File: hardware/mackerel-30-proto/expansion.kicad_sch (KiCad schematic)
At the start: 4 parts, among them J14 DIN41612_03x32_ABC, U14 74HC245, U15 74HC245, U16 74HC245

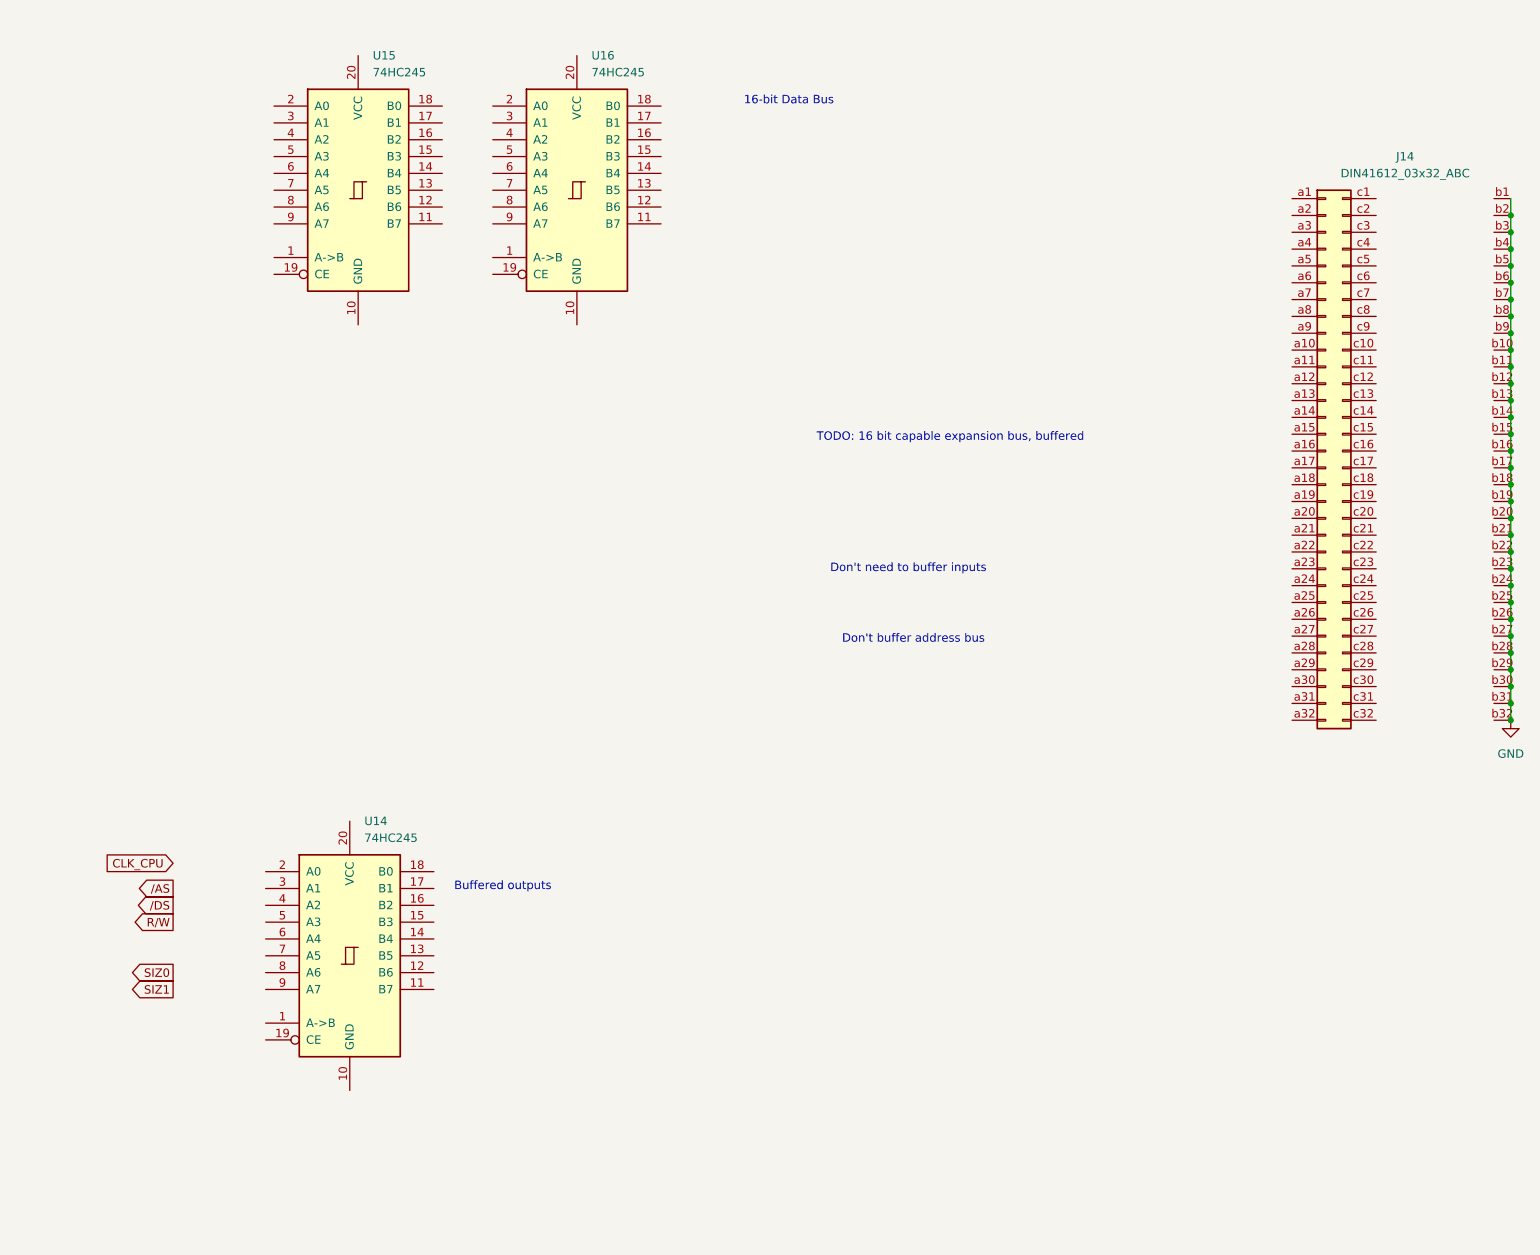
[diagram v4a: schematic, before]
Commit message: Mack-30 routed except for expansion header
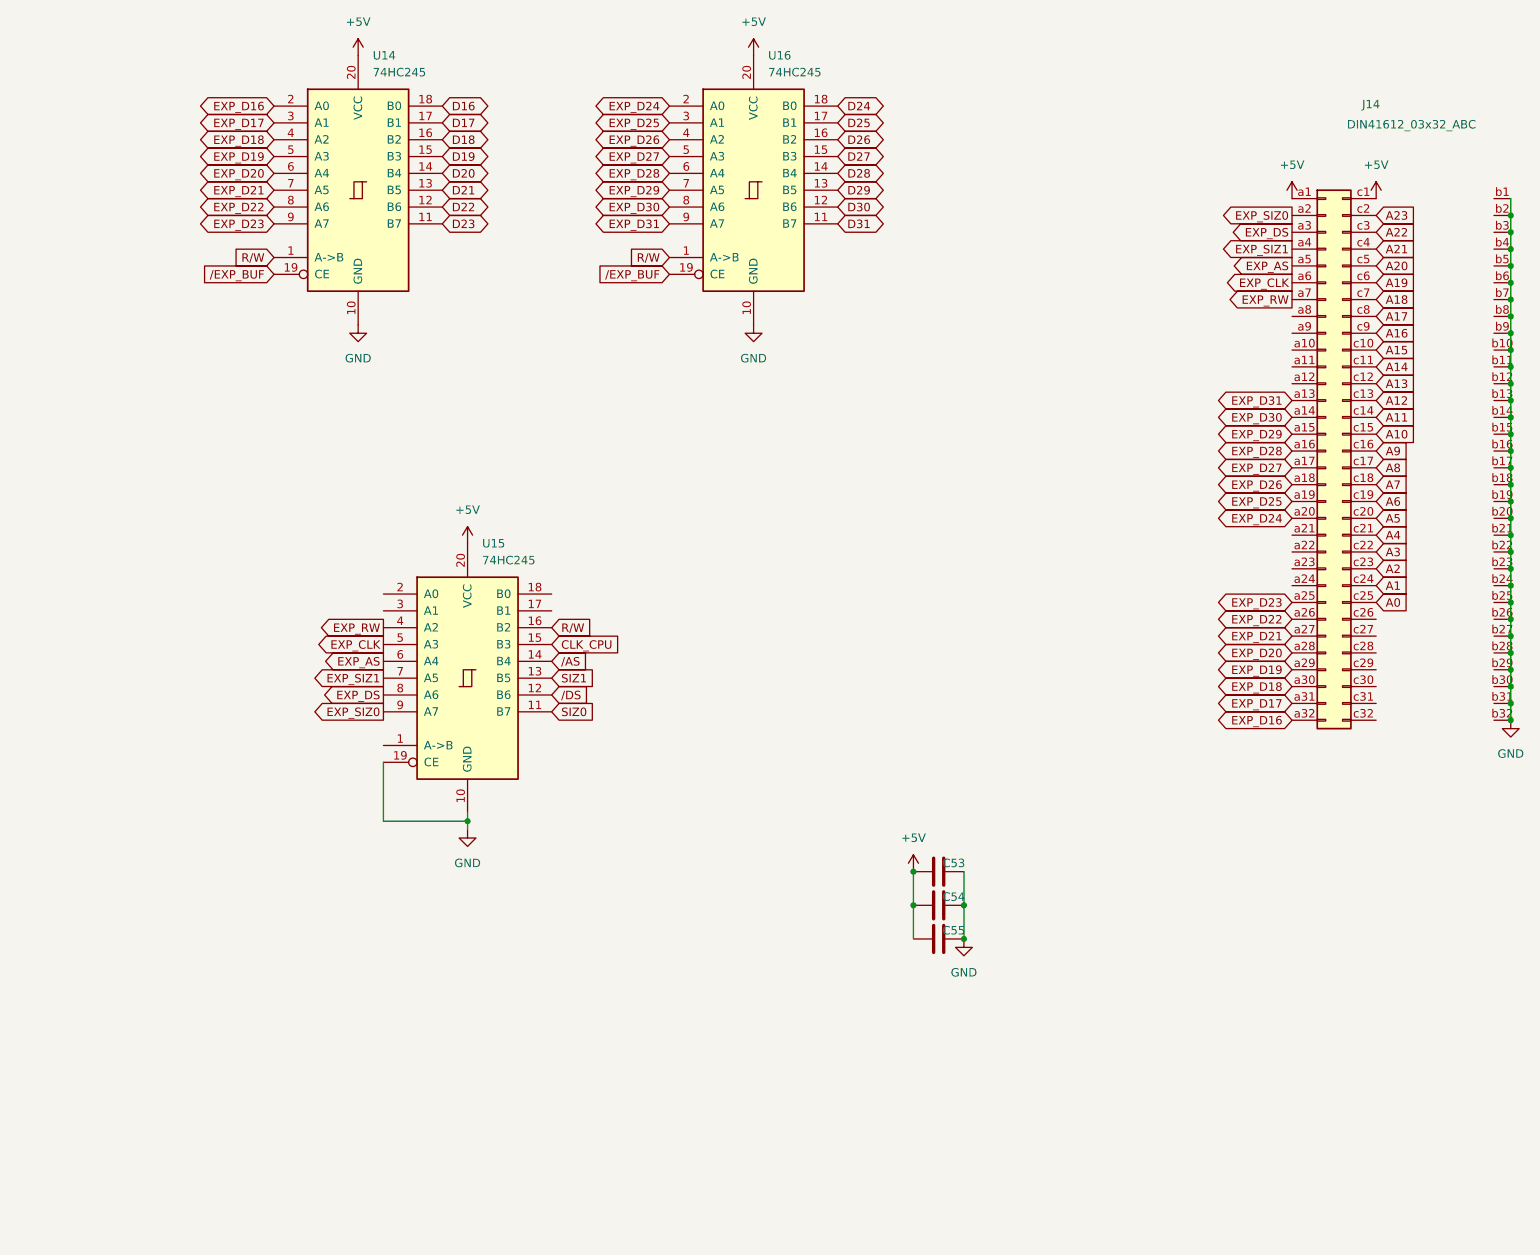
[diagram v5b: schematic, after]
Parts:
- added C53, C54, C55: 0.1uF, Capacitor_THT:C_Disc_D4.3mm_W1.9mm_P5.00mm, symbol Device:C
- renumbered U15 to U14, U14 to U15
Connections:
- net CLK_CPU: now also U15.15 (B3)
- net GND: now also U14.10 (GND), U15.10 (GND), U15.19 (CE), U16.10 (GND), C53.2, C54.2, C55.2
- net R/W: now also U14.1 (A->B), U15.16 (B2), U16.1 (A->B)
- net SIZ0: now also U15.11 (B7)
- net SIZ1: now also U15.13 (B5)
- net /AS: now also U15.14 (B4)
- net /DS: now also U15.12 (B6)
- net +5V: now reaches U15.20 (VCC)
- net +5V: now also J14.a1 (Pin_a1), J14.c1 (Pin_c1), U14.20 (VCC), U16.20 (VCC), C53.1, C54.1, C55.1
- net EXP_RW: now reaches U15.4 (A2)
- net EXP_RW: now also J14.a7 (Pin_a7)
- net EXP_CLK: now reaches U15.5 (A3)
- net EXP_CLK: now also J14.a6 (Pin_a6)
- net EXP_AS: now reaches U15.6 (A4)
- net EXP_AS: now also J14.a5 (Pin_a5)
- net EXP_SIZ1: now reaches U15.7 (A5)
- net EXP_SIZ1: now also J14.a4 (Pin_a4)
- net EXP_DS: now reaches U15.8 (A6)
- net EXP_DS: now also J14.a3 (Pin_a3)
- net EXP_SIZ0: now reaches U15.9 (A7)
- net EXP_SIZ0: now also J14.a2 (Pin_a2)
- net D23: now reaches U14.11 (B7)
- net D22: now reaches U14.12 (B6)
- net D21: now reaches U14.13 (B5)
- net D20: now reaches U14.14 (B4)
- net D19: now reaches U14.15 (B3)
- net D18: now reaches U14.16 (B2)
- net D17: now reaches U14.17 (B1)
- net D16: now reaches U14.18 (B0)
- net /EXP_BUF: now reaches U14.19 (CE)
- net /EXP_BUF: now also U16.19 (CE)
- net EXP_D16: now reaches U14.2 (A0)
- net EXP_D16: now also J14.a32 (Pin_a32)
- net EXP_D17: now reaches U14.3 (A1)
- net EXP_D17: now also J14.a31 (Pin_a31)
- net EXP_D18: now reaches U14.4 (A2)
- net EXP_D18: now also J14.a30 (Pin_a30)
- net EXP_D19: now reaches U14.5 (A3)
- net EXP_D19: now also J14.a29 (Pin_a29)
- net EXP_D20: now reaches U14.6 (A4)
- net EXP_D20: now also J14.a28 (Pin_a28)
- net EXP_D21: now reaches U14.7 (A5)
- net EXP_D21: now also J14.a27 (Pin_a27)
- net EXP_D22: now reaches U14.8 (A6)
- net EXP_D22: now also J14.a26 (Pin_a26)
- net EXP_D23: now reaches U14.9 (A7)
- net EXP_D23: now also J14.a25 (Pin_a25)
- net D31: now reaches U16.11 (B7)
- net D30: now reaches U16.12 (B6)
- net D29: now reaches U16.13 (B5)
- net D28: now reaches U16.14 (B4)
- net D27: now reaches U16.15 (B3)
- net D26: now reaches U16.16 (B2)
- net D25: now reaches U16.17 (B1)
- net D24: now reaches U16.18 (B0)
- net EXP_D24: now reaches U16.2 (A0)
- net EXP_D24: now also J14.a20 (Pin_a20)
- net EXP_D25: now reaches U16.3 (A1)
- net EXP_D25: now also J14.a19 (Pin_a19)
- net EXP_D26: now reaches U16.4 (A2)
- net EXP_D26: now also J14.a18 (Pin_a18)
- net EXP_D27: now reaches U16.5 (A3)
- net EXP_D27: now also J14.a17 (Pin_a17)
- net EXP_D28: now reaches U16.6 (A4)
- net EXP_D28: now also J14.a16 (Pin_a16)
- net EXP_D29: now reaches U16.7 (A5)
- net EXP_D29: now also J14.a15 (Pin_a15)
- net EXP_D30: now reaches U16.8 (A6)
- net EXP_D30: now also J14.a14 (Pin_a14)
- net EXP_D31: now reaches U16.9 (A7)
- net EXP_D31: now also J14.a13 (Pin_a13)
- net A15: now reaches J14.c10 (Pin_c10)
- net A14: now reaches J14.c11 (Pin_c11)
- net A13: now reaches J14.c12 (Pin_c12)
- net A12: now reaches J14.c13 (Pin_c13)
- net A11: now reaches J14.c14 (Pin_c14)
- net A10: now reaches J14.c15 (Pin_c15)
- net A9: now reaches J14.c16 (Pin_c16)
- net A8: now reaches J14.c17 (Pin_c17)
- net A7: now reaches J14.c18 (Pin_c18)
- net A6: now reaches J14.c19 (Pin_c19)
- net A23: now reaches J14.c2 (Pin_c2)
- net A5: now reaches J14.c20 (Pin_c20)
- net A4: now reaches J14.c21 (Pin_c21)
- net A3: now reaches J14.c22 (Pin_c22)
- net A2: now reaches J14.c23 (Pin_c23)
- net A1: now reaches J14.c24 (Pin_c24)
- net A0: now reaches J14.c25 (Pin_c25)
- net A22: now reaches J14.c3 (Pin_c3)
- net A21: now reaches J14.c4 (Pin_c4)
- net A20: now reaches J14.c5 (Pin_c5)
- net A19: now reaches J14.c6 (Pin_c6)
- net A18: now reaches J14.c7 (Pin_c7)
- net A17: now reaches J14.c8 (Pin_c8)
- net A16: now reaches J14.c9 (Pin_c9)
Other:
- note removed: "16-bit Data Bus"
- note removed: "Buffered outputs"
- note removed: "Don't buffer address bus"
- note removed: "Don't need to buffer inputs"
- note removed: "TODO: 16 bit capable expansion bus, buffered"
- moved on the sheet: U15, U16

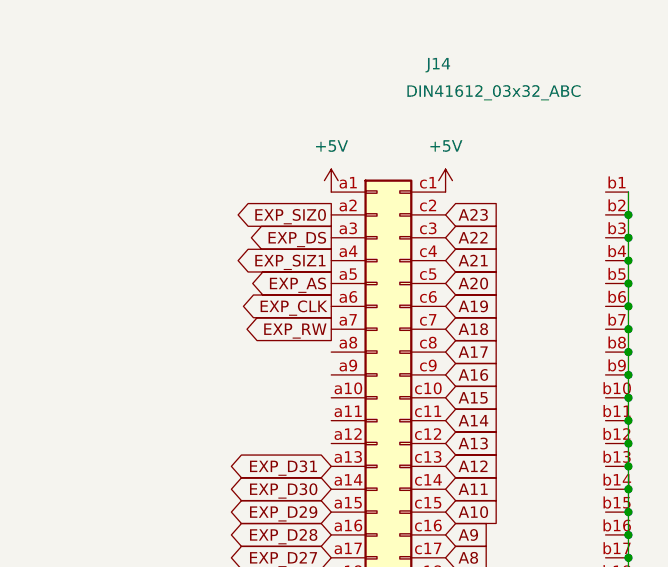
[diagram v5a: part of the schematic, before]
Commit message: Expansion header routed
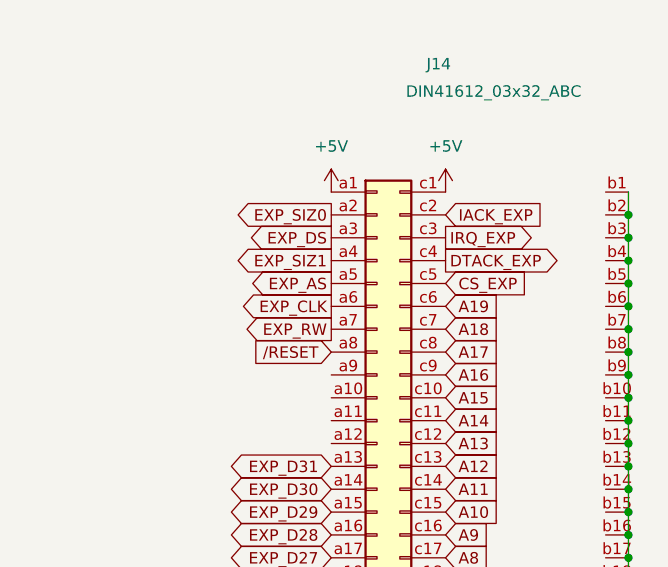
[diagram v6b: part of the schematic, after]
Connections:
- net /RESET: now reaches J14.a8 (Pin_a8)
- net A20 renamed CS_EXP
- net A21 renamed DTACK_EXP
- net A22 renamed IRQ_EXP
- net A23 renamed IACK_EXP
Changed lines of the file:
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@@
-		)
-	)
-	(global_label "A21"
-		(shape input)
-		(at 194.31 54.61 0)
-		(fields_autoplaced yes)
-		(effects
-			(font
-				(size 1.27 1.27)
-			)
-			(justify left)
-		)
-		(property "Intersheetrefs" "${INTERSHEET_REFS}"
-			(at 200.8028 54.61 0)
-			(effects
-				(font
-					(size 1.27 1.27)
-				)
-				(justify left)
-				(hide yes)
-			)
 		)
 	)
@@
 		)
 	)
+	(global_label "IRQ_EXP"
+		(shape output)
+		(at 194.31 52.07 0)
+		(fields_autoplaced yes)
+		(effects
+			(font
+				(size 1.27 1.27)
+			)
+			(justify left)
+		)
+		(property "Intersheetrefs" "${INTERSHEET_REFS}"
+			(at 205.0966 52.07 0)
+			(effects
+				(font
+					(size 1.27 1.27)
+				)
+				(justify left)
+				(hide yes)
+			)
+		)
+	)
 	(global_label "D28"
 		(shape bidirectional)
@@
 		)
 	)
-	(global_label "A20"
-		(shape input)
-		(at 194.31 57.15 0)
-		(fields_autoplaced yes)
-		(effects
-			(font
-				(size 1.27 1.27)
-			)
-			(justify left)
-		)
-		(property "Intersheetrefs" "${INTERSHEET_REFS}"
-			(at 200.8028 57.15 0)
-			(effects
-				(font
-					(size 1.27 1.27)
-				)
-				(justify left)
-				(hide yes)
-			)
-		)
-	)
 	(global_label "A2"
 		(shape input)
@@
 		)
 	)
+	(global_label "{slash}RESET"
+		(shape input)
+		(at 181.61 64.77 180)
+		(fields_autoplaced yes)
+		(effects
+			(font
+				(size 1.27 1.27)
+			)
+			(justify right)
+		)
+		(property "Intersheetrefs" "${INTERSHEET_REFS}"
+			(at 171.5492 64.77 0)
+			(effects
+				(font
+					(size 1.27 1.27)
+				)
+				(justify right)
+				(hide yes)
+			)
+		)
+	)
 	(global_label "A11"
 		(shape input)
@@
 		(property "Intersheetrefs" "${INTERSHEET_REFS}"
 			(at 199.5933 90.17 0)
-			(effects
-				(font
-					(size 1.27 1.27)
-				)
-				(justify left)
-				(hide yes)
-			)
-		)
-	)
-	(global_label "A23"
-		(shape input)
-		(at 194.31 49.53 0)
-		(fields_autoplaced yes)
-		(effects
-			(font
-				(size 1.27 1.27)
-			)
-			(justify left)
-		)
-		(property "Intersheetrefs" "${INTERSHEET_REFS}"
-			(at 200.8028 49.53 0)
 			(effects
 				(font
@@
 		)
 	)
+	(global_label "IACK_EXP"
+		(shape input)
+		(at 194.31 49.53 0)
+		(fields_autoplaced yes)
+		(effects
+			(font
+				(size 1.27 1.27)
+			)
+			(justify left)
+		)
+		(property "Intersheetrefs" "${INTERSHEET_REFS}"
+			(at 206.1247 49.53 0)
+			(effects
+				(font
+					(size 1.27 1.27)
+				)
+				(justify left)
+				(hide yes)
+			)
+		)
+	)
 	(global_label "A16"
 		(shape input)
@@
 		)
 	)
-	(global_label "A22"
-		(shape input)
-		(at 194.31 52.07 0)
-		(fields_autoplaced yes)
-		(effects
-			(font
-				(size 1.27 1.27)
-			)
-			(justify left)
-		)
-		(property "Intersheetrefs" "${INTERSHEET_REFS}"
-			(at 200.8028 52.07 0)
-			(effects
-				(font
-					(size 1.27 1.27)
-				)
-				(justify left)
-				(hide yes)
-			)
-		)
-	)
 	(global_label "A8"
 		(shape input)
@@
 		(property "Intersheetrefs" "${INTERSHEET_REFS}"
 			(at 200.8028 77.47 0)
+			(effects
+				(font
+					(size 1.27 1.27)
+				)
+				(justify left)
+				(hide yes)
+			)
+		)
+	)
+	(global_label "CS_EXP"
+		(shape input)
+		(at 194.31 57.15 0)
+		(fields_autoplaced yes)
+		(effects
+			(font
+				(size 1.27 1.27)
+			)
+			(justify left)
+		)
+		(property "Intersheetrefs" "${INTERSHEET_REFS}"
+			(at 204.3708 57.15 0)
 			(effects
 				(font
@@
 				(hide yes)
 			)
+		)
+	)
+	(global_label "DTACK_EXP"
+		(shape output)
+		(at 194.31 54.61 0)
+		(fields_autoplaced yes)
+		(effects
+			(font
+				(size 1.27 1.27)
+			)
+			(justify left)
+		)
+		(property "Intersheetrefs" "${INTERSHEET_REFS}"
+			(at 207.7575 54.61 0)
+			(effects
+				(font
+					(size 1.27 1.27)
+				)
+				(justify left)
+				(hide yes)
+			)

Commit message: PCB cleanup
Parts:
- added C53, C57: 470uF, Capacitor_THT:CP_Radial_D8.0mm_P3.50mm, symbol Device:C_Polarized_US
- renumbered C53 to C54, C54 to C55, C55 to C56
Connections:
- net +5V: now also C53.1
- net GND: now also U15.1 (A->B), U15.17 (B1), U15.18 (B0), C53.2, C57.2
- net +3.3V: now reaches J14.c32 (Pin_c32)
- net +3.3V: now also C57.1
- no-connect marks 0 -> 16
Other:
- title: Mackerel-30 Proto -> Mackerel-30
